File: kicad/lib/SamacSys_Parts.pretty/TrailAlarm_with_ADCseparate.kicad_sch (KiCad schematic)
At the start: 33 parts, among them IC1 MAX865EUA+T, J1 Conn_01x03, J2 Conn_01x01_Male, J3 Adafruit ADS1115, J4 Bat, Q1 2N3904, SW1 SW_DIP_x01, U1 TLC274, U2 TL074, U3 PocketBeagle

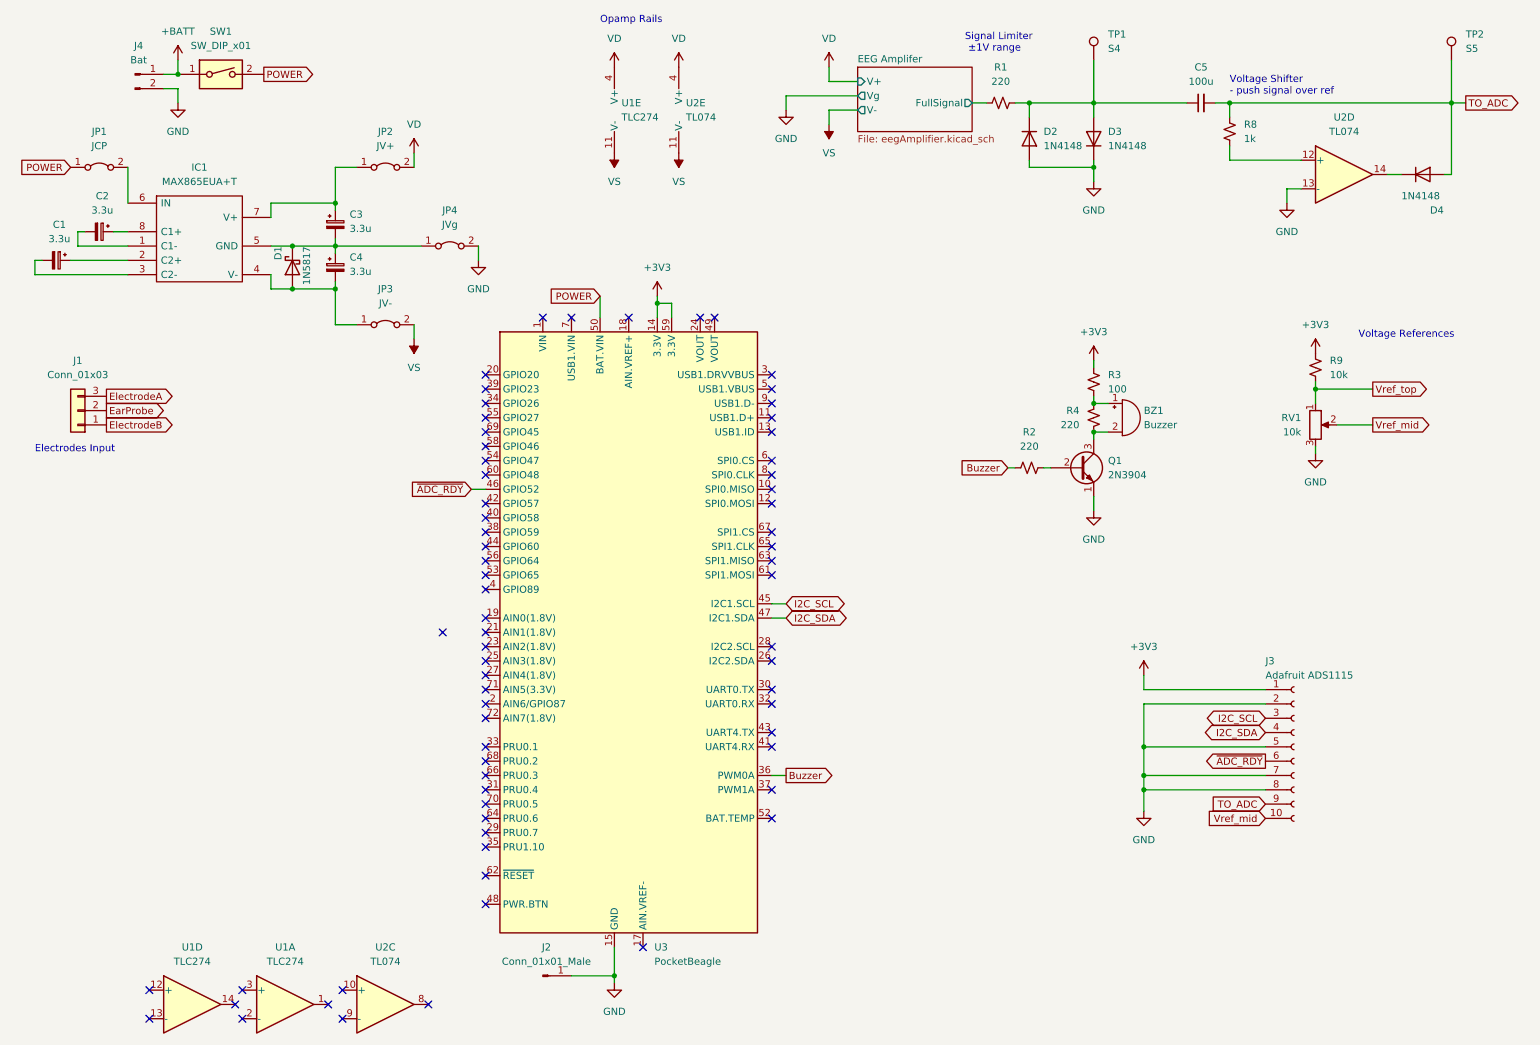
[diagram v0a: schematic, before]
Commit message: Change buzzer pin, i2c pins, ADC plugin, ground pin.
- Change buzzer PWM pin for easier routing.
- Use i2c1 on P2_9(SCL) and P2_11(SDA)
- Use ADS1115 breakout board via header
- Add ground pin next to test points.
- Add header for battery.
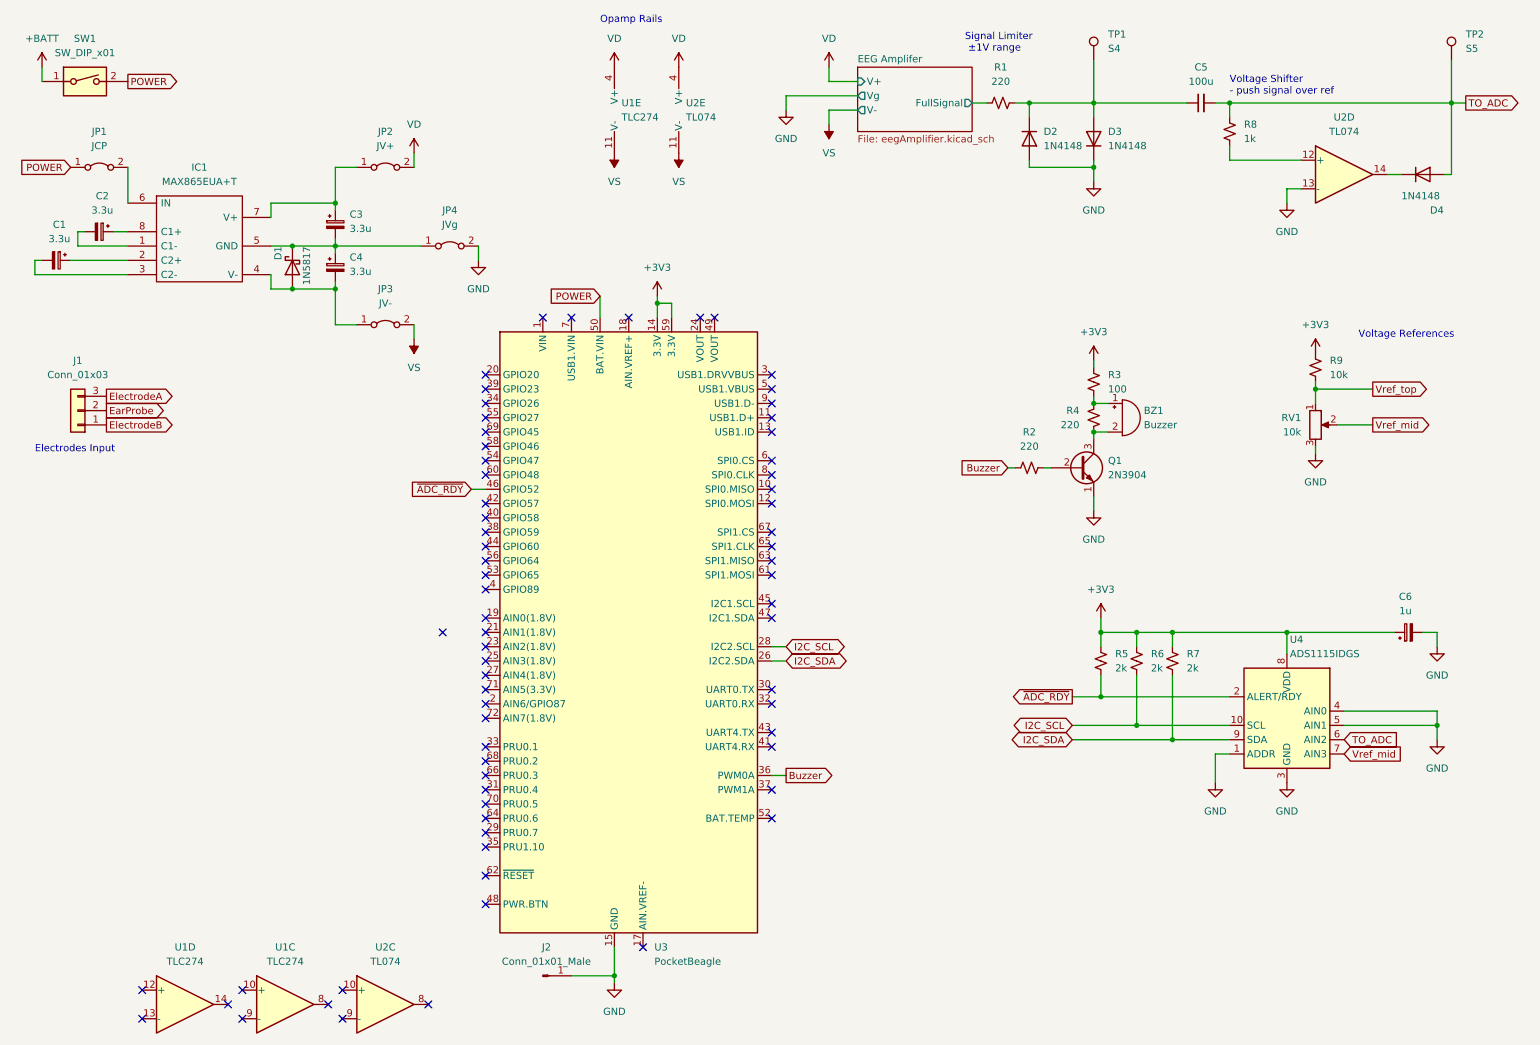
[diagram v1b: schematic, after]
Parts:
- removed J3: Adafruit ADS1115, Connector_PinHeader_2.54mm:PinHeader_1x10_P2.54mm_Vertical, symbol Connector:Conn_01x10_Female
- removed J4: Bat, Connector_PinHeader_2.54mm:PinHeader_1x02_P2.54mm_Vertical, symbol Connector:Conn_01x02_Male
- removed unit 1 of U1
- added C6: 1u, Capacitor_THT:CP_Radial_D4.0mm_P1.50mm, symbol Device:C_Polarized_Small
- added R5, R6, R7: 2k, Resistor_SMD:R_1206_3216Metric_Pad1.30x1.75mm_HandSolder, symbol Device:R_Small_US
- added unit 3 of U1
- added U4: ADS1115IDGS, Package_SO:TSSOP-10_3x3mm_P0.5mm, symbol Analog_ADC:ADS1115IDGS
- D2, D3, D4: footprint Diode_THT:D_DO-35_SOD27_P5.08mm_Vertical_AnodeUp -> Diode_THT:D_DO-35_SOD27_P7.62mm_Horizontal
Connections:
- net +3V3: now also C6.1, R5.1, R6.1, R7.1, U4.8 (VDD)
- net GND: now also C6.2, U4.1 (ADDR), U4.3 (GND), U4.4 (AIN0), U4.5 (AIN1)
- net I2C_SCL: now also U3.28 (I2C2.SCL), R6.2, U4.10 (SCL); no longer U3.45 (I2C1.SCL)
- net I2C_SDA: now also U3.26 (I2C2.SDA), R7.2, U4.9 (SDA); no longer U3.47 (I2C1.SDA)
- net TO_ADC: now also U4.6 (AIN2)
- net Vref_mid: now also U4.7 (AIN3)
- net ~{ADC_RDY}: now also R5.2, U4.2 (ALERT/RDY)
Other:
- moved on the sheet: SW1, U1D
